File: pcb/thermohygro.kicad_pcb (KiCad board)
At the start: 2 copper layers, 50.8 x 43.2 mm, 9 parts, among them J1 RJ45_Shielded, J2 RJ45_Shielded, J3 SSD1306, U1 XIAO-ESP32-S3

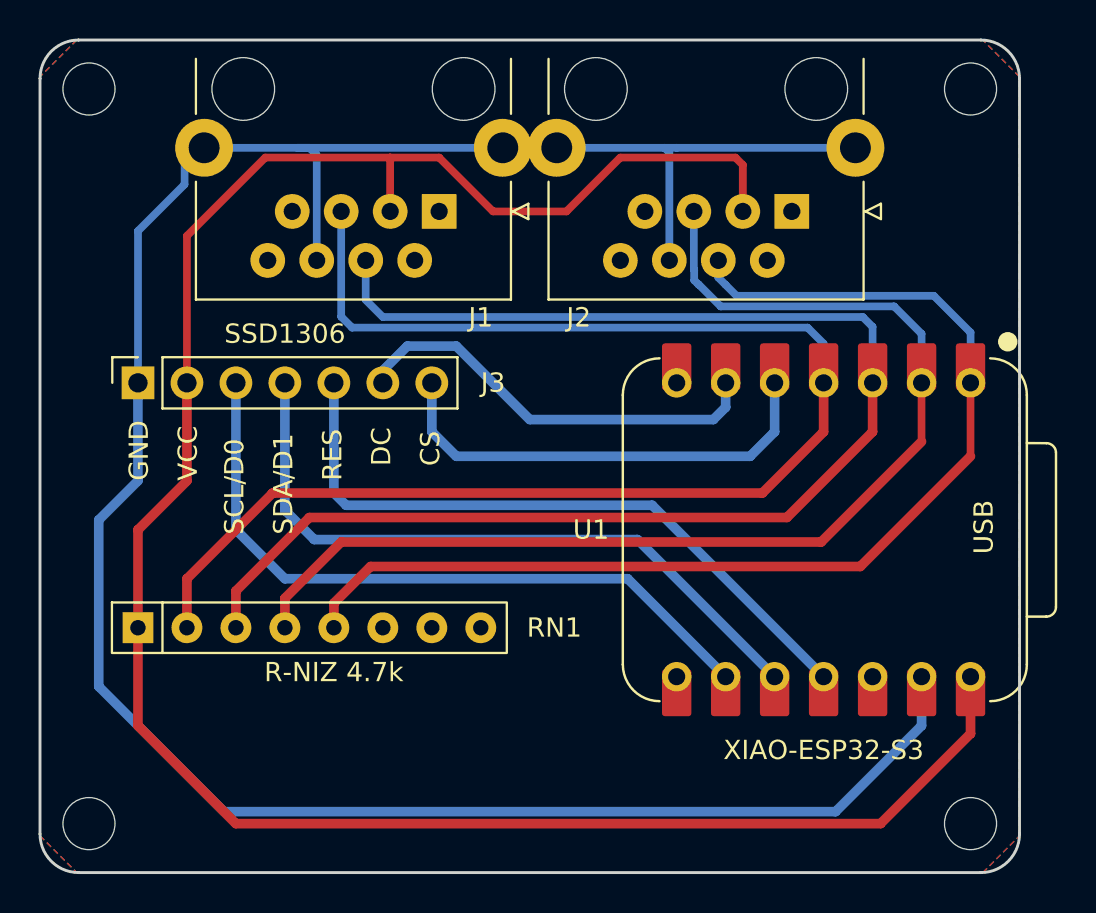
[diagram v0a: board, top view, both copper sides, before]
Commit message: pullup for display i2c
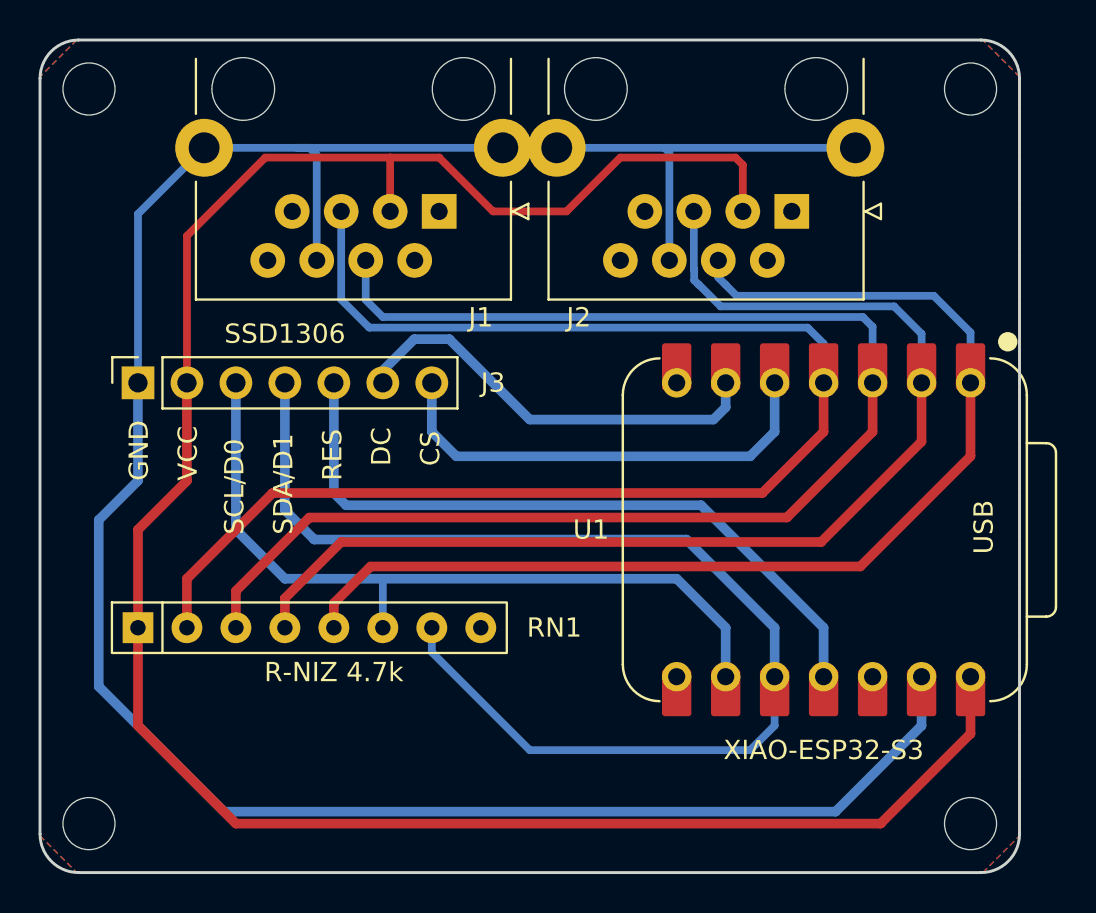
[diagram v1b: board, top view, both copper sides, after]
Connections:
- RN1 pad 6: unconnected-(RN1-R5-Pad6) -> /D0
- RN1 pad 7: unconnected-(RN1-R6-Pad7) -> /D1
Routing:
- net /D1: track 35.6 -> 61.3 mm
- net /D0: track 36.2 -> 40.2 mm
- net /RES: track 35.1 -> 36.5 mm
- net GND: track 127.3 -> 126.3 mm
- net /SDA1: track 74.3 -> 73.8 mm
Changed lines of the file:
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@@
 			(layers "*.Cu" "*.Mask")
 			(remove_unused_layers no)
-			(net "unconnected-(RN1-R5-Pad6)")
+			(net "/D0")
 			(pinfunction "R5_6")
 			(pintype "passive")
@@
 			(layers "*.Cu" "*.Mask")
 			(remove_unused_layers no)
-			(net "unconnected-(RN1-R6-Pad7)")
+			(net "/D1")
 			(pinfunction "R6_7")
 			(pintype "passive")
@@
 	)
 	(segment
+		(start 68.97 107.41)
+		(end 63.511 107.41)
+		(width 0.4)
+		(layer "B.Cu")
+		(net "GND")
+	)
+	(segment
 		(start 64.54 141.84)
 		(end 58.048 135.348)
@@
 	)
 	(segment
+		(start 87.385 107.41)
+		(end 97.289 107.41)
+		(width 0.4)
+		(layer "B.Cu")
+		(net "GND")
+	)
+	(segment
 		(start 100.72 134.84)
 		(end 100.72 137.38)
@@
 	)
 	(segment
-		(start 87.385 107.41)
-		(end 88.02 107.41)
-		(width 0.4)
-		(layer "B.Cu")
-		(net "GND")
-	)
-	(segment
 		(start 77.985 107.41)
 		(end 82.18 107.41)
@@
 	)
 	(segment
+		(start 63.511 107.41)
+		(end 60.08 110.841)
+		(width 0.4)
+		(layer "B.Cu")
+		(net "GND")
+	)
+	(segment
 		(start 58.048 135.348)
 		(end 58.048 126.712)
@@
 	)
 	(segment
-		(start 62.495 107.41)
-		(end 62.495 109.311)
-		(width 0.4)
-		(layer "B.Cu")
-		(net "GND")
-	)
-	(segment
 		(start 69.351 107.791)
 		(end 68.97 107.41)
@@
 	)
 	(segment
-		(start 60.08 111.726)
+		(start 60.08 110.841)
 		(end 60.08 119.092)
-		(width 0.4)
-		(layer "B.Cu")
-		(net "GND")
-	)
-	(segment
-		(start 62.495 109.311)
-		(end 60.08 111.726)
 		(width 0.4)
 		(layer "B.Cu")
@@
 	)
 	(segment
-		(start 88.02 107.41)
-		(end 97.67 107.41)
-		(width 0.4)
-		(layer "B.Cu")
-		(net "GND")
-	)
-	(segment
 		(start 82.18 107.41)
 		(end 87.385 107.41)
@@
 	)
 	(segment
-		(start 62.495 107.41)
-		(end 68.97 107.41)
-		(width 0.4)
-		(layer "B.Cu")
-		(net "GND")
-	)
-	(segment
 		(start 96.26 141.84)
 		(end 64.54 141.84)
@@
 	)
 	(segment
-		(start 90.56 134.84)
-		(end 85.48 129.76)
-		(width 0.5)
-		(layer "B.Cu")
-		(net "/D0")
-	)
-	(segment
 		(start 67.7 129.76)
 		(end 65.16 127.22)
@@
 	)
 	(segment
-		(start 85.48 129.76)
+		(start 72.78 129.76)
 		(end 67.7 129.76)
 		(width 0.5)
@@
 	)
 	(segment
+		(start 90.56 134.84)
+		(end 90.56 132.3)
+		(width 0.5)
+		(layer "B.Cu")
+		(net "/D0")
+	)
+	(segment
+		(start 72.78 132.3)
+		(end 72.78 129.76)
+		(width 0.4)
+		(layer "B.Cu")
+		(net "/D0")
+	)
+	(segment
+		(start 88.02 129.76)
+		(end 72.78 129.76)
+		(width 0.5)
+		(layer "B.Cu")
+		(net "/D0")
+	)
+	(segment
+		(start 90.56 132.3)
+		(end 88.02 129.76)
+		(width 0.5)
+		(layer "B.Cu")
+		(net "/D0")
+	)
+	(segment
+		(start 93.1 137.38)
+		(end 93.1 134.84)
+		(width 0.4)
+		(layer "B.Cu")
+		(net "/D1")
+	)
+	(segment
+		(start 93.1 134.84)
+		(end 93.1 132.3)
+		(width 0.5)
+		(layer "B.Cu")
+		(net "/D1")
+	)
+	(segment
+		(start 88.528 127.728)
+		(end 69.224 127.728)
+		(width 0.5)
+		(layer "B.Cu")
+		(net "/D1")
+	)
+	(segment
+		(start 67.7 126.204)
+		(end 67.7 119.6)
+		(width 0.5)
+		(layer "B.Cu")
+		(net "/D1")
+	)
+	(segment
+		(start 75.32 133.57)
+		(end 80.4 138.65)
+		(width 0.4)
+		(layer "B.Cu")
+		(net "/D1")
+	)
+	(segment
+		(start 93.1 132.3)
+		(end 88.528 127.728)
+		(width 0.5)
+		(layer "B.Cu")
+		(net "/D1")
+	)
+	(segment
+		(start 80.4 138.65)
+		(end 91.83 138.65)
+		(width 0.4)
+		(layer "B.Cu")
+		(net "/D1")
+	)
+	(segment
+		(start 75.32 132.3)
+		(end 75.32 133.57)
+		(width 0.4)
+		(layer "B.Cu")
+		(net "/D1")
+	)
+	(segment
 		(start 69.224 127.728)
 		(end 67.7 126.204)
@@
 	)
 	(segment
-		(start 67.7 126.204)
-		(end 67.7 119.6)
-		(width 0.5)
+		(start 91.83 138.65)
+		(end 93.1 137.38)
+		(width 0.4)
 		(layer "B.Cu")
 		(net "/D1")
 	)
 	(segment
-		(start 85.988 127.728)
-		(end 69.224 127.728)
-		(width 0.5)
-		(layer "B.Cu")
-		(net "/D1")
-	)
-	(segment
-		(start 93.1 134.84)
-		(end 85.988 127.728)
-		(width 0.5)
-		(layer "B.Cu")
-		(net "/D1")
+		(start 70.24 125.315)
+		(end 70.24 119.6)
+		(width 0.5)
+		(layer "B.Cu")
+		(net "/RES")
+	)
+	(segment
+		(start 95.64 134.84)
+		(end 95.64 132.3)
+		(width 0.5)
+		(layer "B.Cu")
+		(net "/RES")
+	)
+	(segment
+		(start 89.29 125.95)
+		(end 70.875 125.95)
+		(width 0.5)
+		(layer "B.Cu")
+		(net "/RES")
 	)
 	(segment
@@
 	)
 	(segment
-		(start 86.75 125.95)
-		(end 70.875 125.95)
-		(width 0.5)
-		(layer "B.Cu")
-		(net "/RES")
-	)
-	(segment
-		(start 70.24 125.315)
-		(end 70.24 119.6)
-		(width 0.5)
-		(layer "B.Cu")
-		(net "/RES")
-	)
-	(segment
-		(start 95.64 134.84)
-		(end 86.75 125.95)
+		(start 95.64 132.3)
+		(end 89.29 125.95)
 		(width 0.5)
 		(layer "B.Cu")
@@
 	)
 	(segment
-		(start 72.78 118.965)
-		(end 74.05 117.695)
-		(width 0.5)
-		(layer "B.Cu")
-		(net "/DC")
-	)
-	(segment
-		(start 76.59 117.695)
-		(end 80.4 121.505)
+		(start 72.78 119.6)
+		(end 72.78 118.965)
 		(width 0.5)
 		(layer "B.Cu")
@@
 	)
 	(segment
-		(start 74.05 117.695)
-		(end 76.59 117.695)
-		(width 0.5)
-		(layer "B.Cu")
-		(net "/DC")
-	)
-	(segment
-		(start 72.78 119.6)
-		(end 72.78 118.965)
-		(width 0.5)
-		(layer "B.Cu")
-		(net "/DC")
-	)
-	(segment
 		(start 89.925 121.505)
 		(end 90.56 120.87)
@@
 	)
 	(segment
+		(start 74.409 117.336)
+		(end 76.231 117.336)
+		(width 0.5)
+		(layer "B.Cu")
+		(net "/DC")
+	)
+	(segment
+		(start 72.78 118.965)
+		(end 74.409 117.336)
+		(width 0.5)
+		(layer "B.Cu")
+		(net "/DC")
+	)
+	(segment
+		(start 76.231 117.336)
+		(end 80.4 121.505)
+		(width 0.5)
+		(layer "B.Cu")
+		(net "/DC")
+	)
+	(segment
 		(start 91.83 123.41)
 		(end 93.1 122.14)
@@
 	)
 	(segment
-		(start 70.621 110.71)
-		(end 70.621 116.171)
+		(start 70.621 115.282)
+		(end 72.075 116.736)
+		(width 0.4)
+		(layer "B.Cu")
+		(net "/SDA1")
+	)
+	(segment
+		(start 72.075 116.736)
+		(end 94.808 116.736)
 		(width 0.4)
 		(layer "B.Cu")
@@
 	)
 	(segment
-		(start 70.621 116.171)
-		(end 71.186 116.736)
-		(width 0.4)
-		(layer "B.Cu")
-		(net "/SDA1")
-	)
-	(segment
 		(start 94.808 116.736)
 		(end 95.64 117.568)
@@
 	)
 	(segment
-		(start 71.186 116.736)
-		(end 94.808 116.736)
+		(start 70.621 110.71)
+		(end 70.621 115.282)
 		(width 0.4)
 		(layer "B.Cu")
@@
 		(start 103.26 123.41)
 		(end 103.26 119.6)
-		(width 0.4)
+		(width 0.5)
 		(layer "F.Cu")
 		(net "/SCK2")
@@
 		(start 100.72 122.648)
 		(end 100.72 119.6)
-		(width 0.4)
+		(width 0.5)
 		(layer "F.Cu")
 		(net "/SDA2")

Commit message: fixed fatal PCB failure which permanently destroys SHT85 if plugged. RJ45 pins were reversed and now placed in correct order.
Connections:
- J1 pad 3: +3.3V -> GND
- J1 pad 4: /SCK1 -> /SDA1
- J1 pad 5: /SDA1 -> /SCK1
- J1 pad 6: GND -> +3.3V
- J2 pad 3: +3.3V -> GND
- J2 pad 4: /SCK2 -> /SDA2
- J2 pad 5: /SDA2 -> /SCK2
- J2 pad 6: GND -> +3.3V
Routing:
- net GND: track 126.3 -> 114.2 mm
- net +3.3V: track 114.0 -> 103.6 mm
- net /SCK2: track 59.0 -> 66.5 mm
- net /SCK1: track 72.7 -> 79.7 mm
- net /SDA1: track 73.8 -> 70.1 mm
- net /SDA2: track 59.6 -> 56.7 mm
- added copper zone on F.Cu, net GND
- removed copper zone on F.Cu, net +3.3V
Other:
- board text added: "v1.1"

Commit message: fixed 5V connected wrong instead of 3.3V. Now 3.3V
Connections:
- U1 pad 12: unconnected-(U1-3V3_OUT-Pad12) -> +3.3V
- U1 pad 14: +3.3V -> unconnected-(U1-VBUS-Pad14)
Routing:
- net +3.3V: track 103.6 -> 96.2 mm
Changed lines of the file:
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@@
 	(paper "A4")
 	(title_block
-		(date "2026-09-03")
-		(rev "1.1")
+		(date "2026-09-04")
+		(rev "1.2")
 	)
 	(layers
@@
 			(layers "*.Cu" "*.Mask")
 			(remove_unused_layers no)
-			(net "unconnected-(U1-3V3_OUT-Pad12)")
+			(net "+3.3V")
 			(pinfunction "3V3_OUT_12")
 			(pintype "passive")
@@
 			(layers "F.Cu" "F.Mask")
 			(roundrect_rratio 0.1)
-			(net "unconnected-(U1-3V3_OUT-Pad12)")
+			(net "+3.3V")
 			(pinfunction "3V3_OUT_12")
 			(pintype "passive")
@@
 			(layers "*.Cu" "*.Mask")
 			(remove_unused_layers no)
-			(net "+3.3V")
+			(net "unconnected-(U1-VBUS-Pad14)")
 			(pinfunction "VBUS_14")
 			(pintype "passive")
@@
 			(layers "F.Cu" "F.Mask")
 			(roundrect_rratio 0.1)
-			(net "+3.3V")
+			(net "unconnected-(U1-VBUS-Pad14)")
 			(pinfunction "VBUS_14")
 			(pintype "passive")
@@
 	)
 	(segment
-		(start 103.26 137.7975)
-		(end 98.5975 142.46)
-		(width 0.5)
-		(layer "F.Cu")
-		(net "+3.3V")
-	)
-	(segment
-		(start 60.08 137.38)
-		(end 60.08 132.3)
-		(width 0.5)
-		(layer "F.Cu")
-		(net "+3.3V")
-	)
-	(segment
-		(start 60.08 132.3)
-		(end 60.08 127.22)
-		(width 0.5)
-		(layer "F.Cu")
-		(net "+3.3V")
-	)
-	(segment
 		(start 87.639 115.409)
 		(end 87.639 113.25)
@@
 	)
 	(segment
-		(start 98.5975 142.46)
-		(end 65.16 142.46)
-		(width 0.5)
-		(layer "F.Cu")
-		(net "+3.3V")
-	)
-	(segment
-		(start 103.26 135.675)
-		(end 103.26 137.7975)
-		(width 0.5)
-		(layer "F.Cu")
-		(net "+3.3V")
-	)
-	(segment
 		(start 87.004 116.044)
 		(end 87.639 115.409)
@@
 	)
 	(segment
-		(start 65.16 142.46)
-		(end 60.08 137.38)
-		(width 0.5)
-		(layer "F.Cu")
-		(net "+3.3V")
-	)
-	(segment
-		(start 60.08 127.22)
-		(end 62.62 124.68)
-		(width 0.5)
-		(layer "F.Cu")
-		(net "+3.3V")
-	)
-	(segment
-		(start 62.62 124.68)
-		(end 62.62 119.6)
-		(width 0.5)
-		(layer "F.Cu")
-		(net "+3.3V")
-	)
-	(segment
 		(start 69.351 113.25)
 		(end 69.351 115.409)
@@
 	)
 	(segment
+		(start 98.18 137.38)
+		(end 95.132 140.428)
+		(width 0.4)
+		(layer "B.Cu")
+		(net "+3.3V")
+	)
+	(segment
+		(start 95.132 140.428)
+		(end 65.16 140.428)
+		(width 0.4)
+		(layer "B.Cu")
+		(net "+3.3V")
+	)
+	(segment
 		(start 62.62 116.806)
 		(end 63.382 116.044)
@@
 	)
 	(segment
+		(start 98.18 134.84)
+		(end 98.18 137.38)
+		(width 0.4)
+		(layer "B.Cu")
+		(net "+3.3V")
+	)
+	(segment
+		(start 60.08 127.22)
+		(end 62.62 124.68)
+		(width 0.4)
+		(layer "B.Cu")
+		(net "+3.3V")
+	)
+	(segment
+		(start 65.16 140.428)
+		(end 60.08 135.348)
+		(width 0.4)
+		(layer "B.Cu")
+		(net "+3.3V")
+	)
+	(segment
+		(start 62.62 124.68)
+		(end 62.62 119.6)
+		(width 0.4)
+		(layer "B.Cu")
+		(net "+3.3V")
+	)
+	(segment
 		(start 62.62 119.6)
 		(end 62.62 116.806)
@@
 	)
 	(segment
+		(start 60.08 135.348)
+		(end 60.08 132.3)
+		(width 0.4)
+		(layer "B.Cu")
+		(net "+3.3V")
+	)
+	(segment
 		(start 63.382 116.044)
 		(end 68.716 116.044)
 		(width 0.4)
 		(layer "B.Cu")
+		(net "+3.3V")
+	)
+	(segment
+		(start 60.08 132.3)
+		(end 60.08 127.22)
+		(width 0.4)
+		(layer "B.Cu")

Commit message: updated schematics with 8->10-pin R network, 7->8-pin display connector and additional wire to display
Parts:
- J3: footprint Connector_PinSocket_2.54mm:PinSocket_1x07_P2.54mm_Vertical -> Connector_PinSocket_2.54mm:PinSocket_1x08_P2.54mm_Vertical
- RN1: footprint Resistor_THT:R_Array_SIP8 -> Resistor_THT:R_Array_SIP10
- moved RN1 2.54 mm to (60.1, 134.8)
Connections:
- U1 pad 7: unconnected-(U1-D6-Pad7) -> Net-(J3-Pin_8)
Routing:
- net Net-(J3-Pin_8): track 0.00 -> 10.2 mm
- net /SDA2: track 56.7 -> 59.3 mm
- net /SDA1: track 70.1 -> 72.6 mm
- net /SCK2: track 66.5 -> 69.0 mm
- net /SCK1: track 79.7 -> 82.2 mm
- net /D0: track 40.2 -> 42.7 mm
- net GND: track 114.2 -> 116.1 mm
- net +3.3V: track 96.2 -> 97.5 mm
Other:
- board text added: "v1.2"
- board text removed: "v1.1"
